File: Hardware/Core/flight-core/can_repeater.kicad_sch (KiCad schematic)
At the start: 0 parts

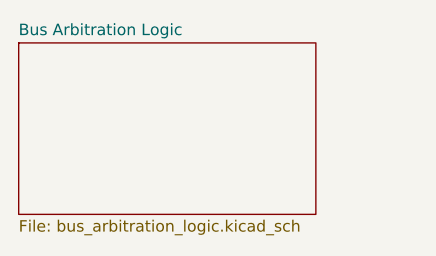
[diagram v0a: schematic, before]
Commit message: moving multi-unit parts into OlinBAD library; added 0603 0.1uF cap
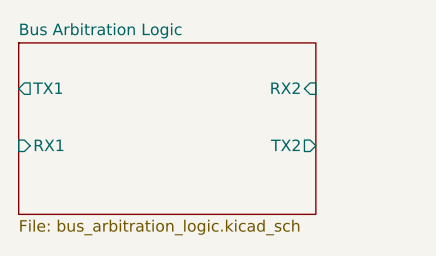
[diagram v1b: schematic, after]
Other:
- sheet Bus Arbitration Logic ports: added RX1, RX2, TX1, TX2; removed none
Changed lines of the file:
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@@
+			)
+		)
+		(pin "TX1" output
+			(at 114.3 82.55 180)
+			(effects
+				(font
+					(size 1.27 1.27)
+				)
+				(justify left)
+			)
+		)
+		(pin "RX2" input
+			(at 147.32 82.55 0)
+			(effects
+				(font
+					(size 1.27 1.27)
+				)
+				(justify right)
+			)
+		)
+		(pin "TX2" output
+			(at 147.32 88.9 0)
+			(effects
+				(font
+					(size 1.27 1.27)
+				)
+				(justify right)
+			)
+		)
+		(pin "RX1" input
+			(at 114.3 88.9 180)
+			(effects
+				(font
+					(size 1.27 1.27)
+				)
+				(justify left)
 			)
 		)

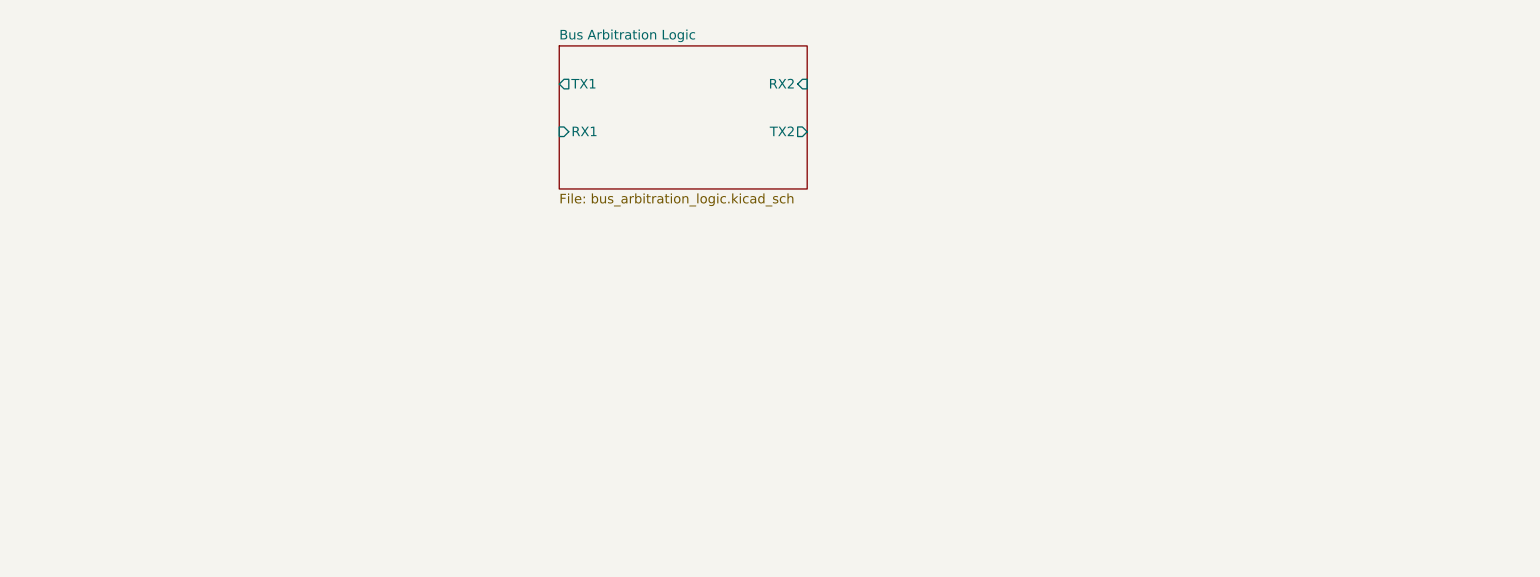
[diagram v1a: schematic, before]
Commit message: Removed images, added 3.3V and 5V hierarchical inputs, added second pair of decoupling caps
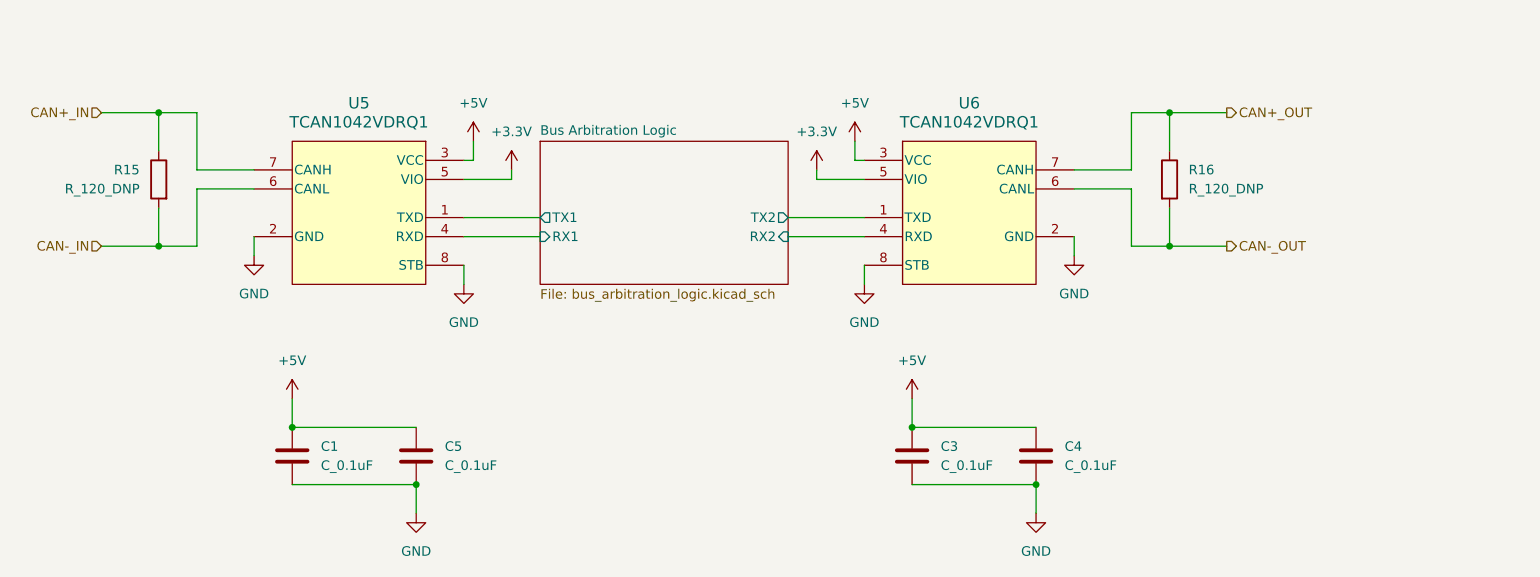
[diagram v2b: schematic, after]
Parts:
- added C1, C3, C4, C5: C_0.1uF, footprints:C_0603_1608Metric, symbol OlinBAD:C_0.1uF_0603
- added R15, R16: R_120_DNP, footprints:R_0805_OEM, symbol formula:R_120_DNP
- added U5, U6: TCAN1042VDRQ1, BAD_LIB:D0008A_M, symbol OlinBAD:TCAN1042VDRQ1
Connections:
- net Bus Arbitration Logic/RX1: now also U5.4 (RXD)
- net Bus Arbitration Logic/RX2: now also U6.4 (RXD)
- net Bus Arbitration Logic/TX1: now also U5.1 (TXD)
- net Bus Arbitration Logic/TX2: now also U6.1 (TXD)
- new net +3.3V: U5.5 (VIO), U6.5 (VIO)
- new net +5V: C1.1, C3.1, C4.1, C5.1, U5.3 (VCC), U6.3 (VCC)
- new net CAN+_IN: R15.1, U5.7 (CANH)
- new net CAN+_OUT: R16.1, U6.7 (CANH)
- new net CAN-_IN: R15.2, U5.6 (CANL)
- new net CAN-_OUT: R16.2, U6.6 (CANL)
- new net GND: C1.2, C3.2, C4.2, C5.2, U5.2 (GND), U5.8 (STB), U6.2 (GND), U6.8 (STB)

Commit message: renaming the values of LRC generics to just the value with unit letter (except resistors are just the value)
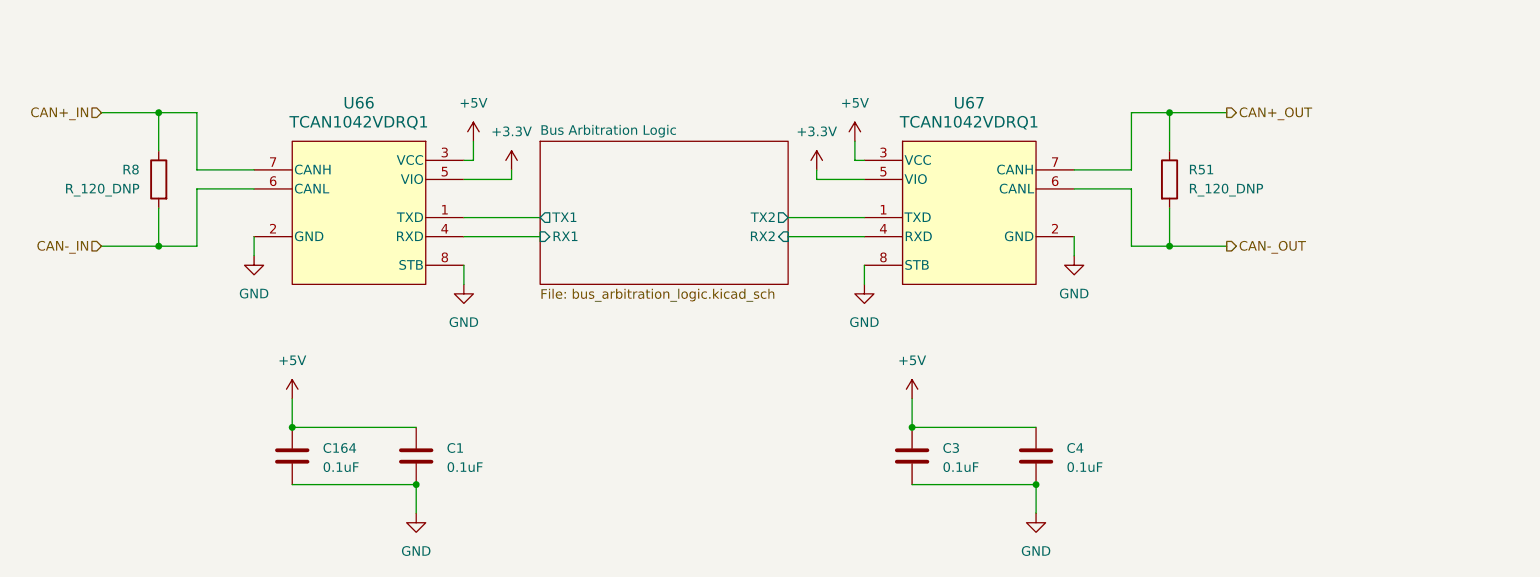
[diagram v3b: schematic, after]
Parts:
- removed C5: C_0.1uF, footprints:C_0603_1608Metric, symbol OlinBAD:C_0.1uF_0603
- added C164: 0.1uF, footprints:C_0603_1608Metric, symbol OlinBAD:C_0.1uF_0603
- C1, C3, C4: value C_0.1uF -> 0.1uF
- renumbered R16 to R51, R15 to R8, U5 to U66, U6 to U67
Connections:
- net +5V: now also C164.1
- net GND: now also C164.2

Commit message: changed tcan to HGVDR variety, changed termination R schematics
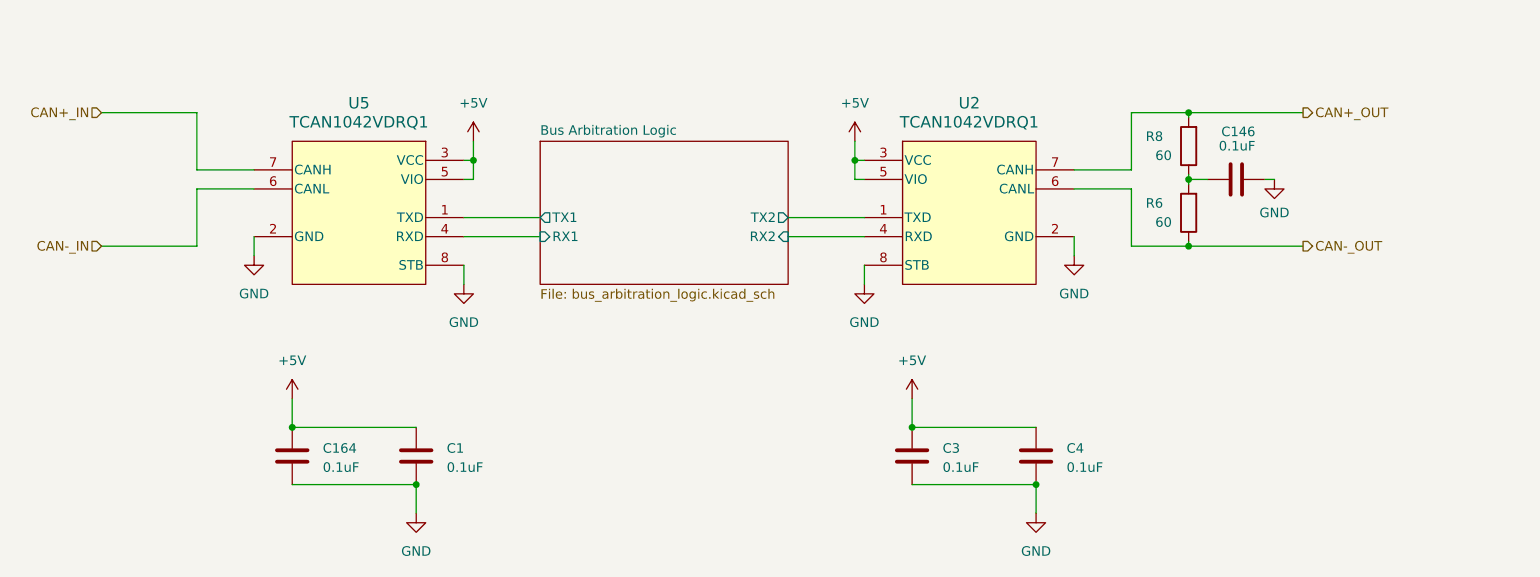
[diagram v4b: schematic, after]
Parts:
- removed R51, R8: R_120_DNP, footprints:R_0805_OEM, symbol formula:R_120_DNP
- removed U66, U67: TCAN1042VDRQ1, BAD_LIB:D0008A_M, symbol OlinBAD:TCAN1042VDRQ1
- added C146: 0.1uF, footprints:C_0603_1608Metric, symbol OlinBAD:C_0.1uF_0603
- added R6, R8: 60, footprints:C_0603_1608Metric, symbol Device:R
- added U2, U5: TCAN1042VDRQ1, obad_footprints:D0008A_M, symbol OlinBAD:TCAN1042HGVDRQ1
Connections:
- net +5V: now also U2.3 (VCC), U2.5 (VIO), U5.3 (VCC), U5.5 (VIO)
- net Bus Arbitration Logic/RX1: now also U5.4 (RXD)
- net Bus Arbitration Logic/RX2: now also U2.4 (RXD)
- net Bus Arbitration Logic/TX1: now also U5.1 (TXD)
- net Bus Arbitration Logic/TX2: now also U2.1 (TXD)
- net CAN+_IN: now also U5.7 (CANH)
- net CAN+_OUT: now also R8.2, U2.7 (CANH)
- net CAN-_IN: now also U5.6 (CANL)
- net CAN-_OUT: now also R6.1, U2.6 (CANL)
- net GND: now also C146.2, U2.2 (GND), U2.8 (STB), U5.2 (GND), U5.8 (STB)
- new net: C146.1, R6.2, R8.1

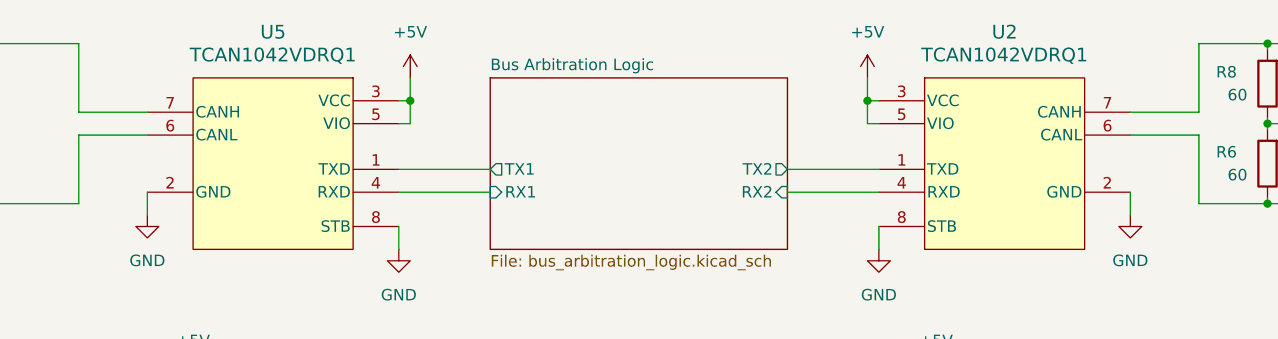
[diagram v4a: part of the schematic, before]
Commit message: fixing incorrect value name for tcan HG part
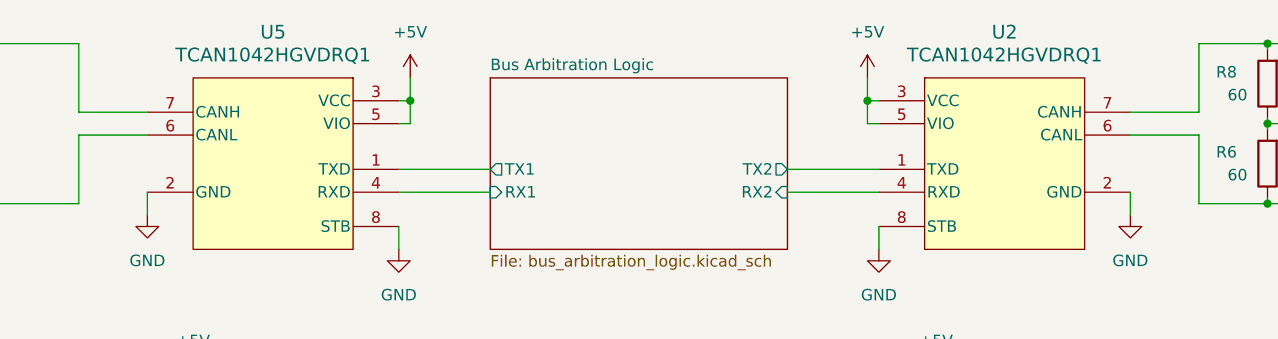
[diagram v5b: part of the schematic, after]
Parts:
- U2, U5: value TCAN1042VDRQ1 -> TCAN1042HGVDRQ1
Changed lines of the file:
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@@
+	)
+	(symbol
+		(lib_id "OlinBAD:TCAN1042HGVDRQ1")
+		(at 87.63 104.14 0)
+		(mirror y)
+		(unit 1)
+		(exclude_from_sim no)
+		(in_bom yes)
+		(on_board yes)
+		(dnp no)
+		(property "Reference" "U5"
+			(at 87.63 85.09 0)
+			(effects
+				(font
+					(size 1.524 1.524)
+				)
+			)
+		)
+		(property "Value" "TCAN1042HGVDRQ1"
+			(at 87.63 87.63 0)
+			(effects
+				(font
+					(size 1.524 1.524)
+				)
+			)
+		)
+		(property "Footprint" "obad_footprints:D0008A_M"
+			(at 87.63 97.536 0)
+			(effects
+				(font
+					(size 1.27 1.27)
+					(italic yes)
+				)
+				(hide yes)
+			)
+		)
+		(property "Datasheet" "https://www.ti.com/lit/ds/symlink/tcan1042hgv-q1.pdf?HQS=dis-dk-null-digikeymode-dsf-pf-null-wwe&ts=1763514572527&ref_url=https%253A%252F%252Fwww.ti.com%252Fgeneral%252Fdocs%252Fsuppproductinfo.tsp%253FdistId%253D10%2526gotoUrl%253Dhttps%253A%252F%252Fwww.ti.com%252Flit%252Fgpn%252Ftcan1042hgv-q1"
+			(at 88.138 96.012 0)
+			(effects
+				(font
+					(size 1.27 1.27)
+					(italic yes)
+				)
+				(hide yes)
+			)
+		)
+		(property "Description" "(VIO 5V) Automotive Fault Protected CAN Transceiver with CAN FD"
+			(at 87.63 104.14 0)
+			(effects
+				(font
+					(size 1.27 1.27)
+				)
+				(hide yes)
+			)
+		)
+		(property "Purchase Link" "https://www.digikey.com/en/products/detail/texas-instruments/TCAN1042HGVDRQ1/5967638?gclsrc=aw.ds&gad_source=1&gad_campaignid=120565755&gbraid=0AAAAADrbLljwAXt-QCRGsfhWJNL9EDDzm&gclid=CjwKCAiAz_DIBhBJEiwAVH2XwHEXN2txZcp9zpCNMQ7T_4r1dgZgYo6IwLw2TloibvoGR3RSDrh8aRoCYN8QAvD_BwE"
+			(at 87.63 104.14 0)
+			(effects
+				(font
+					(size 1.27 1.27)
+				)
+				(hide yes)
+			)
+		)
+		(pin "3"
+		)
+		(pin "5"
+		)
+		(pin "1"
+		)
+		(pin "4"
+		)
+		(pin "8"
+		)
+		(pin "7"
+		)
+		(pin "6"
+		)
+		(pin "2"
+		)
+		(instances
+			(project "flight-core"
+				(path "/93f46f4b-cdf5-47ec-af03-96378e73b2e1/66136be3-edc9-4a2c-bee0-74cf2086e2ec"
+					(reference "U70")
+					(unit 1)
+				)
+				(path "/93f46f4b-cdf5-47ec-af03-96378e73b2e1/8530813e-1c71-4684-b5d7-274038aa1688"
+					(reference "U83")
+					(unit 1)
+				)
+				(path "/93f46f4b-cdf5-47ec-af03-96378e73b2e1/9a54db1a-b47f-4159-981e-de187c4c4ab9"
+					(reference "U85")
+					(unit 1)
+				)
+				(path "/93f46f4b-cdf5-47ec-af03-96378e73b2e1/b78052bb-331a-483e-8ae2-7fb3771b0ac3"
+					(reference "U5")
+					(unit 1)
+				)
+				(path "/93f46f4b-cdf5-47ec-af03-96378e73b2e1/ba3a1bbc-b1e5-484f-8b44-4c2b1cf2999c"
+					(reference "U91")
+					(unit 1)
+				)
+				(path "/93f46f4b-cdf5-47ec-af03-96378e73b2e1/c609f1a1-abda-478b-aae8-3ac690d48591"
+					(reference "U84")
+					(unit 1)
+				)
+				(path "/93f46f4b-cdf5-47ec-af03-96378e73b2e1/7dc5358b-fa42-41f0-aa49-5a04c373b069/0d8aff7f-d6ca-4045-85c5-1a1f4c62101b"
+					(reference "U17")
+					(unit 1)
+				)
+				(path "/93f46f4b-cdf5-47ec-af03-96378e73b2e1/7dc5358b-fa42-41f0-aa49-5a04c373b069/344cc74f-a628-49df-be8a-bc5614ade625"
+					(reference "U9")
+					(unit 1)
+				)
+				(path "/93f46f4b-cdf5-47ec-af03-96378e73b2e1/7dc5358b-fa42-41f0-aa49-5a04c373b069/4d4d4b6e-b0b8-4e7c-8890-6ff279f1bf86"
+					(reference "U15")
+					(unit 1)
+				)
+				(path "/93f46f4b-cdf5-47ec-af03-96378e73b2e1/7dc5358b-fa42-41f0-aa49-5a04c373b069/548c5fda-faed-4907-ac4a-bc470113a7d0"
+					(reference "U7")
+					(unit 1)
+				)
+				(path "/93f46f4b-cdf5-47ec-af03-96378e73b2e1/7dc5358b-fa42-41f0-aa49-5a04c373b069/554781ed-180d-4035-b0cf-be25a87c50d5"
+					(reference "U19")
+					(unit 1)
+				)
+				(path "/93f46f4b-cdf5-47ec-af03-96378e73b2e1/7dc5358b-fa42-41f0-aa49-5a04c373b069/5cd59e90-1b11-4144-87f2-aafe09e96414"
+					(reference "U21")
+					(unit 1)
+				)
+				(path "/93f46f4b-cdf5-47ec-af03-96378e73b2e1/7dc5358b-fa42-41f0-aa49-5a04c373b069/7185d0b4-1971-45be-af29-2a5ca11b78e7"
+					(reference "U23")
+					(unit 1)
+				)
+				(path "/93f46f4b-cdf5-47ec-af03-96378e73b2e1/7dc5358b-fa42-41f0-aa49-5a04c373b069/c8d150bc-4746-43dd-a1b2-8ca0ae03d6a6"
+					(reference "U66")
+					(unit 1)
+				)
+			)
+		)
 	)
 	(symbol
@@
 			)
 		)
-		(property "Value" "TCAN1042VDRQ1"
+		(property "Value" "TCAN1042HGVDRQ1"
 			(at 168.91 87.63 0)
 			(effects
@@
 		(pin "3"
 		)
+		(pin "5"
+		)
+		(pin "1"
+		)
+		(pin "4"
+		)
+		(pin "8"
+		)
+		(pin "7"
+		)
+		(pin "6"
+		)
 		(pin "2"
-		)
-		(pin "1"
-		)
-		(pin "5"
-		)
-		(pin "8"
-		)
-		(pin "4"
-		)
-		(pin "6"
-		)
-		(pin "7"
 		)
 		(instances
@@
 					(unit 1)
 				)
-			)
-		)
-	)
-	(symbol
-		(lib_id "OlinBAD:TCAN1042HGVDRQ1")
-		(at 87.63 104.14 0)
-		(mirror y)
-		(unit 1)
-		(exclude_from_sim no)
-		(in_bom yes)
-		(on_board yes)
-		(dnp no)
-		(property "Reference" "U5"
-			(at 87.63 85.09 0)
-			(effects
-				(font
-					(size 1.524 1.524)
-				)
-			)
-		)
-		(property "Value" "TCAN1042VDRQ1"
-			(at 87.63 87.63 0)
-			(effects
-				(font
-					(size 1.524 1.524)
-				)
-			)
-		)
-		(property "Footprint" "obad_footprints:D0008A_M"
-			(at 87.63 97.536 0)
-			(effects
-				(font
-					(size 1.27 1.27)
-					(italic yes)
-				)
-				(hide yes)
-			)
-		)
-		(property "Datasheet" "https://www.ti.com/lit/ds/symlink/tcan1042hgv-q1.pdf?HQS=dis-dk-null-digikeymode-dsf-pf-null-wwe&ts=1763514572527&ref_url=https%253A%252F%252Fwww.ti.com%252Fgeneral%252Fdocs%252Fsuppproductinfo.tsp%253FdistId%253D10%2526gotoUrl%253Dhttps%253A%252F%252Fwww.ti.com%252Flit%252Fgpn%252Ftcan1042hgv-q1"
-			(at 88.138 96.012 0)
-			(effects
-				(font
-					(size 1.27 1.27)
-					(italic yes)
-				)
-				(hide yes)
-			)
-		)
-		(property "Description" "(VIO 5V) Automotive Fault Protected CAN Transceiver with CAN FD"
-			(at 87.63 104.14 0)
-			(effects
-				(font
-					(size 1.27 1.27)
-				)
-				(hide yes)
-			)
-		)
-		(property "Purchase Link" "https://www.digikey.com/en/products/detail/texas-instruments/TCAN1042HGVDRQ1/5967638?gclsrc=aw.ds&gad_source=1&gad_campaignid=120565755&gbraid=0AAAAADrbLljwAXt-QCRGsfhWJNL9EDDzm&gclid=CjwKCAiAz_DIBhBJEiwAVH2XwHEXN2txZcp9zpCNMQ7T_4r1dgZgYo6IwLw2TloibvoGR3RSDrh8aRoCYN8QAvD_BwE"
-			(at 87.63 104.14 0)
-			(effects
-				(font
-					(size 1.27 1.27)
-				)
-				(hide yes)
-			)
-		)
-		(pin "3"
-		)
-		(pin "2"
-		)
-		(pin "1"
-		)
-		(pin "5"
-		)
-		(pin "8"
-		)
-		(pin "4"
-		)
-		(pin "6"
-		)
-		(pin "7"
-		)
-		(instances
-			(project "flight-core"
-				(path "/93f46f4b-cdf5-47ec-af03-96378e73b2e1/66136be3-edc9-4a2c-bee0-74cf2086e2ec"
-					(reference "U70")
-					(unit 1)
-				)
-				(path "/93f46f4b-cdf5-47ec-af03-96378e73b2e1/8530813e-1c71-4684-b5d7-274038aa1688"
-					(reference "U83")
-					(unit 1)
-				)
-				(path "/93f46f4b-cdf5-47ec-af03-96378e73b2e1/9a54db1a-b47f-4159-981e-de187c4c4ab9"
-					(reference "U85")
-					(unit 1)
-				)
-				(path "/93f46f4b-cdf5-47ec-af03-96378e73b2e1/b78052bb-331a-483e-8ae2-7fb3771b0ac3"
-					(reference "U5")
-					(unit 1)
-				)
-				(path "/93f46f4b-cdf5-47ec-af03-96378e73b2e1/ba3a1bbc-b1e5-484f-8b44-4c2b1cf2999c"
-					(reference "U91")
-					(unit 1)
-				)
-				(path "/93f46f4b-cdf5-47ec-af03-96378e73b2e1/c609f1a1-abda-478b-aae8-3ac690d48591"
-					(reference "U84")
-					(unit 1)
-				)
-				(path "/93f46f4b-cdf5-47ec-af03-96378e73b2e1/7dc5358b-fa42-41f0-aa49-5a04c373b069/0d8aff7f-d6ca-4045-85c5-1a1f4c62101b"
-					(reference "U17")
-					(unit 1)
-				)
-				(path "/93f46f4b-cdf5-47ec-af03-96378e73b2e1/7dc5358b-fa42-41f0-aa49-5a04c373b069/344cc74f-a628-49df-be8a-bc5614ade625"
-					(reference "U9")
-					(unit 1)
-				)
-				(path "/93f46f4b-cdf5-47ec-af03-96378e73b2e1/7dc5358b-fa42-41f0-aa49-5a04c373b069/4d4d4b6e-b0b8-4e7c-8890-6ff279f1bf86"
-					(reference "U15")
-					(unit 1)
-				)
-				(path "/93f46f4b-cdf5-47ec-af03-96378e73b2e1/7dc5358b-fa42-41f0-aa49-5a04c373b069/548c5fda-faed-4907-ac4a-bc470113a7d0"
-					(reference "U7")
-					(unit 1)
-				)
-				(path "/93f46f4b-cdf5-47ec-af03-96378e73b2e1/7dc5358b-fa42-41f0-aa49-5a04c373b069/554781ed-180d-4035-b0cf-be25a87c50d5"
-					(reference "U19")
-					(unit 1)
-				)
-				(path "/93f46f4b-cdf5-47ec-af03-96378e73b2e1/7dc5358b-fa42-41f0-aa49-5a04c373b069/5cd59e90-1b11-4144-87f2-aafe09e96414"
-					(reference "U21")
-					(unit 1)
-				)
-				(path "/93f46f4b-cdf5-47ec-af03-96378e73b2e1/7dc5358b-fa42-41f0-aa49-5a04c373b069/7185d0b4-1971-45be-af29-2a5ca11b78e7"
-					(reference "U23")
-					(unit 1)
-				)
-				(path "/93f46f4b-cdf5-47ec-af03-96378e73b2e1/7dc5358b-fa42-41f0-aa49-5a04c373b069/c8d150bc-4746-43dd-a1b2-8ca0ae03d6a6"
-					(reference "U66")
-					(unit 1)
-				)

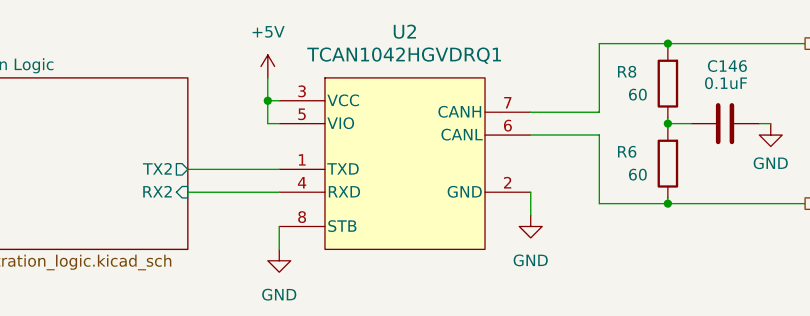
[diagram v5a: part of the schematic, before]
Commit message: updated shutdown and some aux circuits
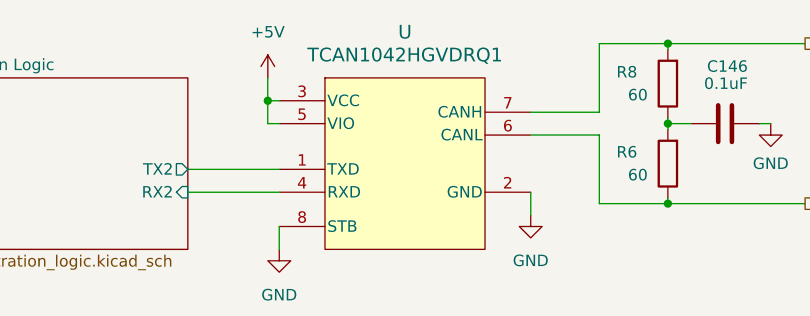
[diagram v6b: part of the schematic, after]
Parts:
- renumbered U2 to U

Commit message: updated all top sheets
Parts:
- renumbered U to U?
